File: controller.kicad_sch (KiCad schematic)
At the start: 32 parts, among them J1 Conn_01x06_Female, J2 Conn_01x022_Male, J20 Conn_01x06_Female

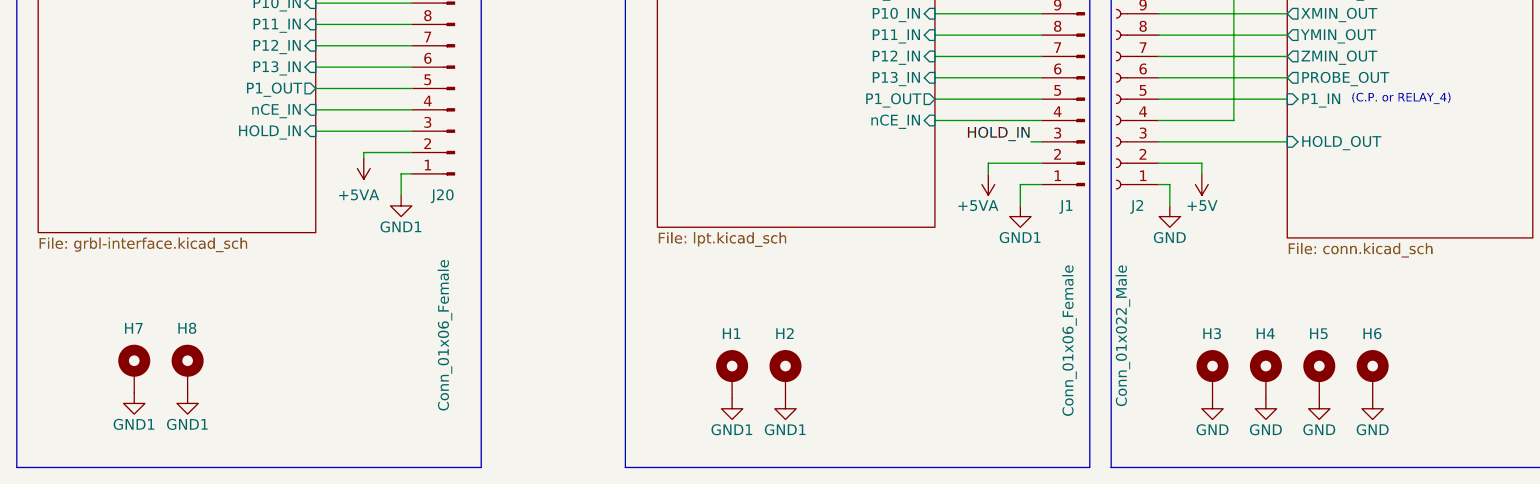
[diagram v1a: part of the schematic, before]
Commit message: Optical isolator input current (10mA not 3mA) and wiring error fixed.
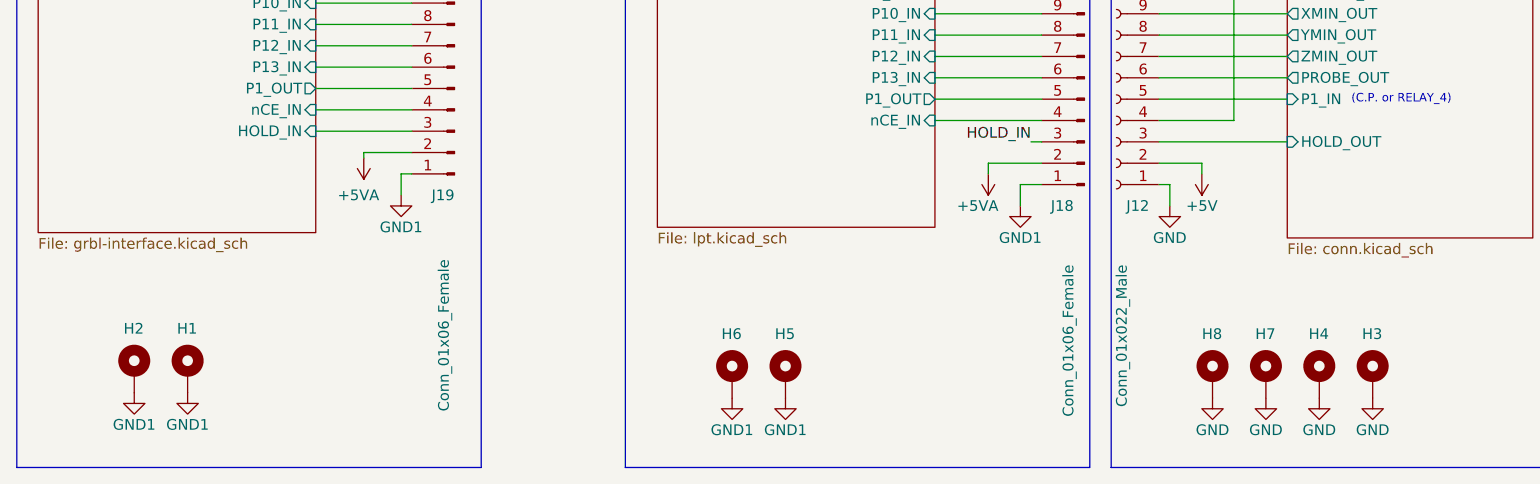
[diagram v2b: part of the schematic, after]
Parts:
- renumbered H8 to H1, H7 to H2, H6 to H3, H5 to H4, H2 to H5, H1 to H6, H4 to H7, H3 to H8, J2 to J12, J1 to J18, J20 to J19

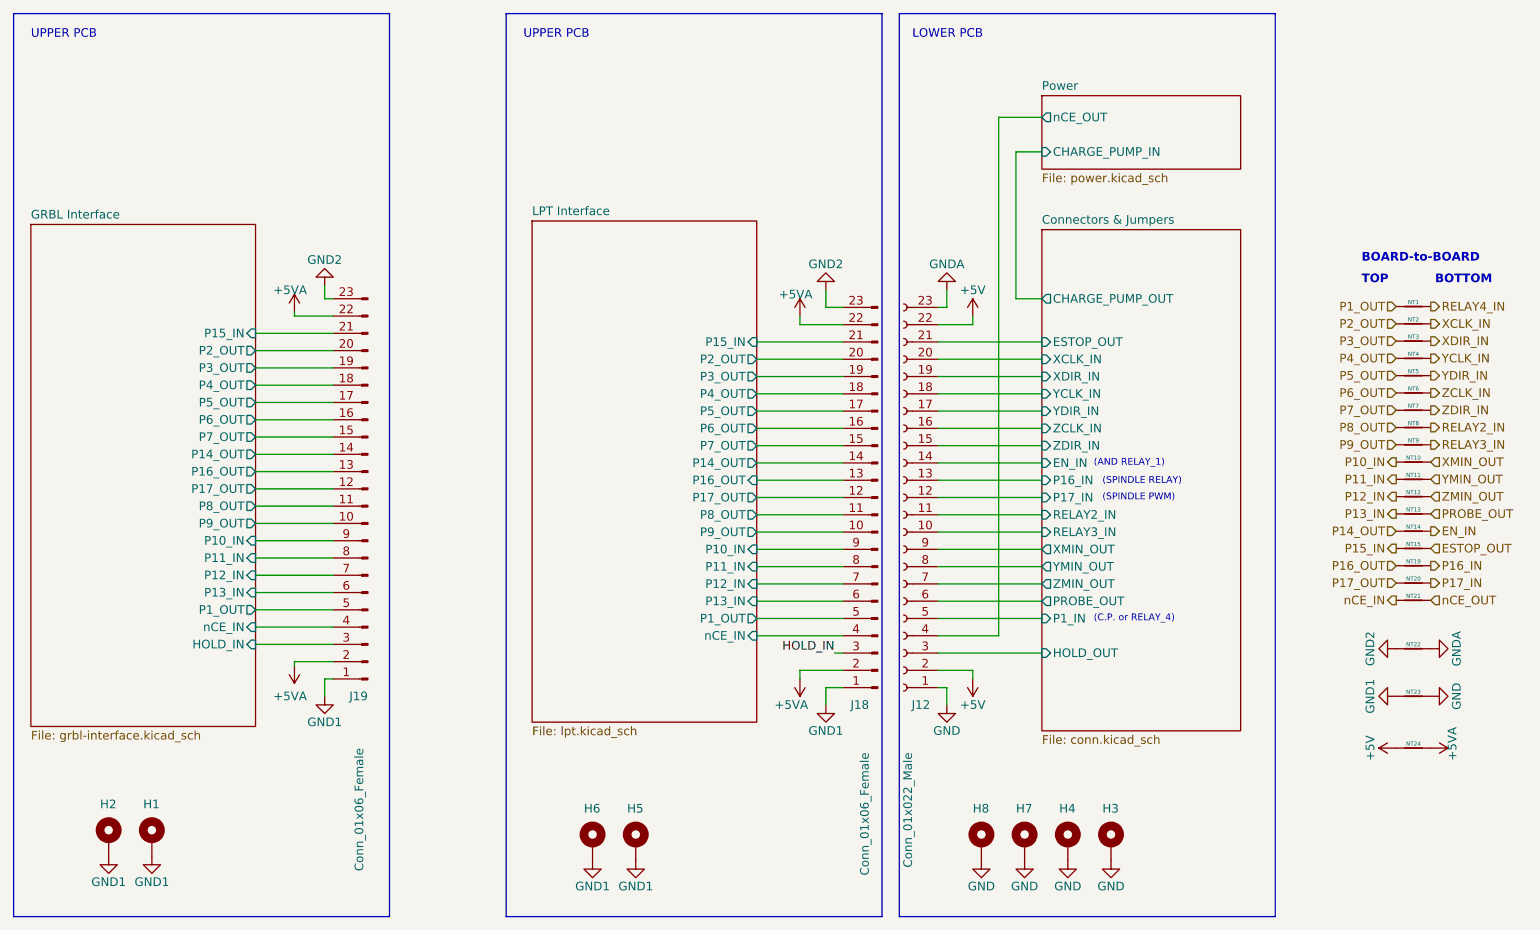
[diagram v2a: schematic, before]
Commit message: Multiple flaws resolved
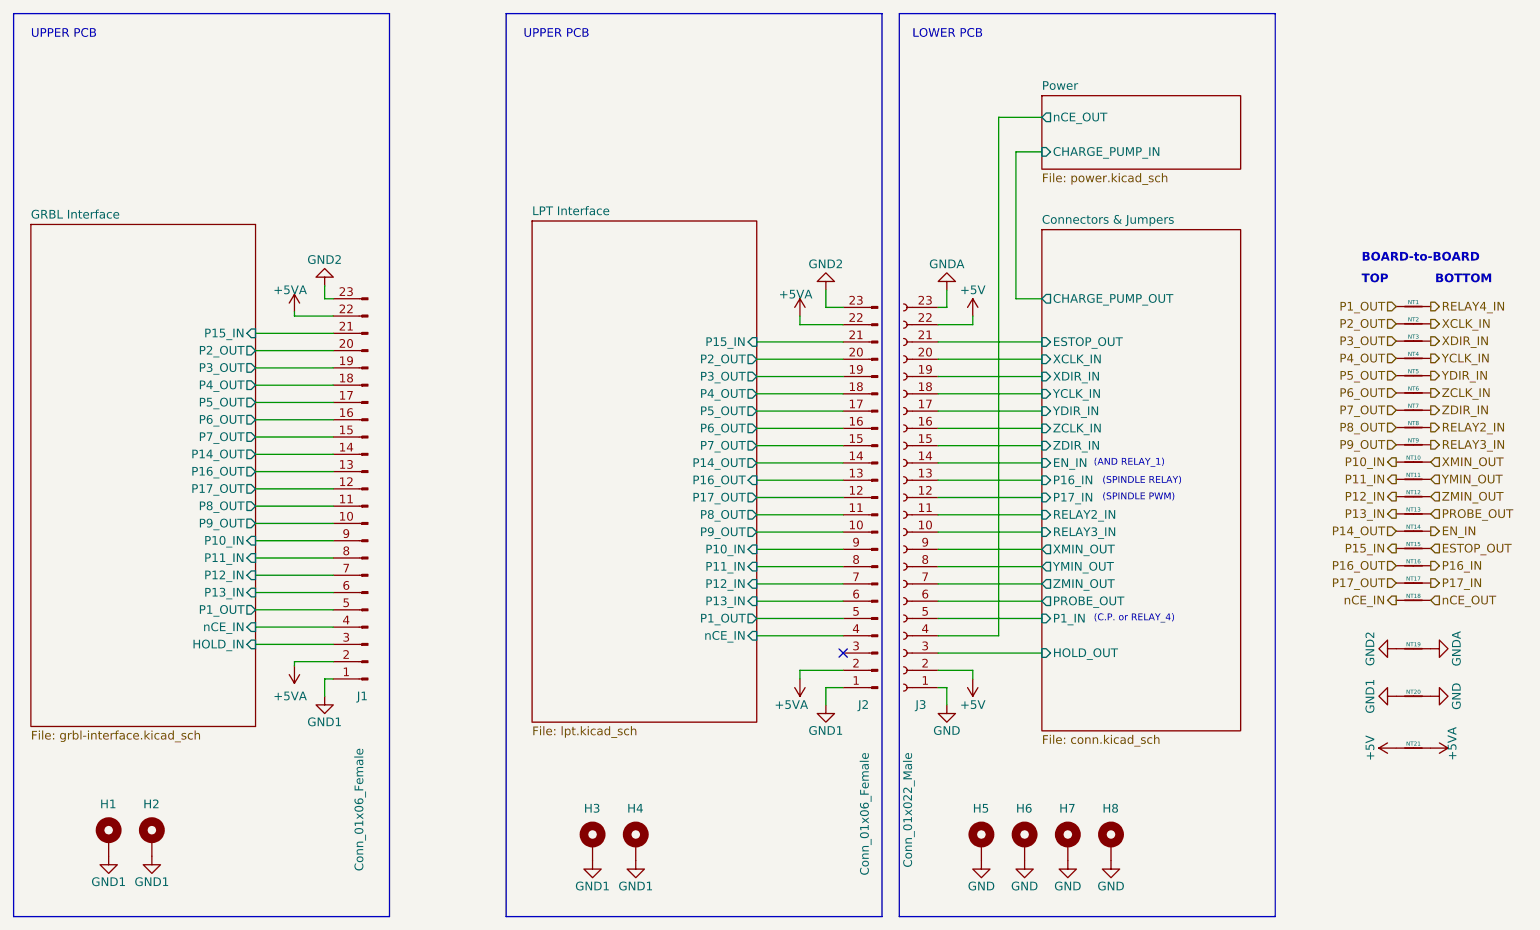
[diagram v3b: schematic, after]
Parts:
- renumbered H2 to H1, H1 to H2, H6 to H3, H5 to H4, H8 to H5, H7 to H6, H4 to H7, H3 to H8, J19 to J1, J18 to J2, J12 to J3, NT19 to NT16, NT20 to NT17, NT21 to NT18, NT22 to NT19, NT23 to NT20, NT24 to NT21
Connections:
- net HOLD_IN: no longer names the net of J2.3 (Pin_3)
- no-connect marks 0 -> 1

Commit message: Oh ... just a few more fuckups fixed
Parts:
- removed NT1, NT10, NT11, NT12, NT13, NT14, NT15, NT16, NT17, NT18, NT2, NT3, NT4, NT5, NT6, NT7, NT8, NT9: NetTie_2, -Project:NetTie-2_SMD_Pad0.3mm, symbol Device:NetTie_2
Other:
- note removed: "BOARD-to-BOARD"
- note removed: "BOTTOM"
- note removed: "TOP"
